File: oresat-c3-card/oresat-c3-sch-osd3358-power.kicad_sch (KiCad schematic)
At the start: 39 parts, among them Q6 MMBT2907, U1 OSD3358-1G-ISM, U10 SN74AUC1G07DCKR, U14 TLVH431

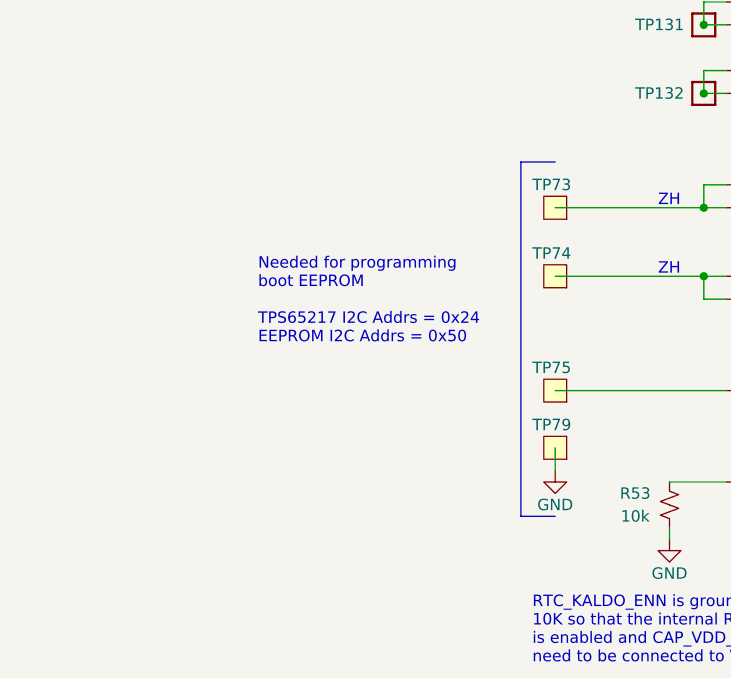
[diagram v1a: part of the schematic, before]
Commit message: schematic changes following design review
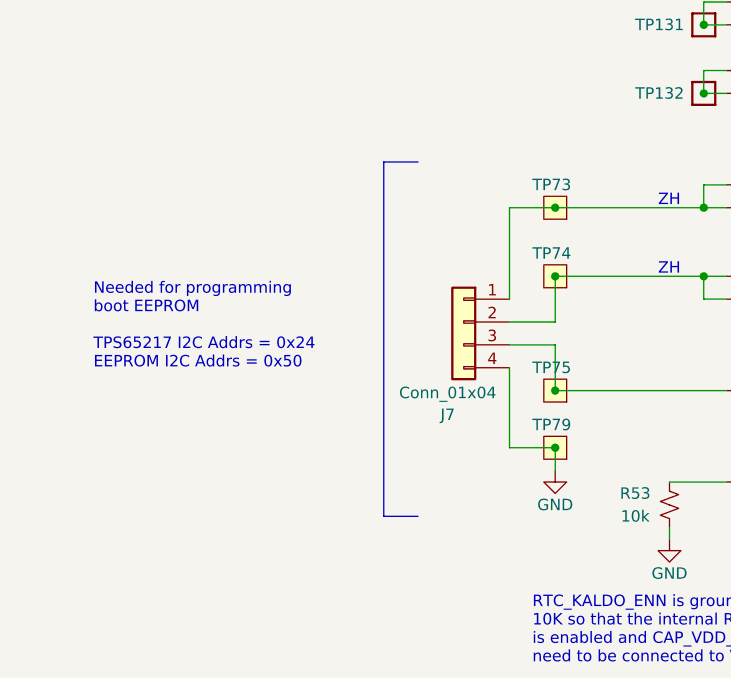
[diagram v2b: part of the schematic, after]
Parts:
- added J7: Conn_01x04, symbol Connector_Generic:Conn_01x04
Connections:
- net GND: now also J7.4 (Pin_4)
- net at TP75.1, U1.M2 (EEPROM_WP): now also J7.3 (Pin_3)
- net at TP74.1, U1.C11 (I2C0_SDA), U1.D11 (PMIC_SDA): now also J7.2 (Pin_2)
- net at TP73.1, U1.C10 (I2C0_SCL), U1.D10 (PMIC_SCL): now also J7.1 (Pin_1)
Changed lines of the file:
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@@
 	(text "Needed for programming\nboot EEPROM\n\nTPS65217 I2C Addrs = 0x24\nEEPROM I2C Addrs = 0x50"
 		(exclude_from_sim no)
-		(at 137.16 200.66 0)
+		(at 118.872 203.454 0)
 		(effects
 			(font
@@
 	)
 	(junction
+		(at 170.18 205.74)
+		(diameter 0)
+		(color 0 0 0 0)
+	)
+	(junction
 		(at 186.69 55.88)
 		(diameter 0)
@@
 	)
 	(junction
+		(at 170.18 185.42)
+		(diameter 0)
+		(color 0 0 0 0)
+	)
+	(junction
 		(at 265.43 157.48)
 		(diameter 0)
@@
 	)
 	(junction
+		(at 170.18 212.09)
+		(diameter 0)
+		(color 0 0 0 0)
+	)
+	(junction
 		(at 292.1 215.9)
 		(diameter 0)
@@
 	)
 	(junction
+		(at 170.18 193.04)
+		(diameter 0)
+		(color 0 0 0 0)
+	)
+	(junction
 		(at 265.43 149.86)
 		(diameter 0)
@@
 	(wire
 		(pts
+			(xy 170.18 200.66) (xy 170.18 205.74)
+		)
+		(stroke
+			(width 0)
+			(type default)
+		)
+	)
+	(wire
+		(pts
 			(xy 299.72 207.01) (xy 299.72 208.28)
 		)
@@
 	(polyline
 		(pts
-			(xy 166.37 219.71) (xy 170.18 219.71)
+			(xy 151.13 219.71) (xy 154.94 219.71)
 		)
 		(stroke
@@
 	(polyline
 		(pts
-			(xy 170.18 180.34) (xy 166.37 180.34)
+			(xy 154.94 180.34) (xy 151.13 180.34)
 		)
 		(stroke
@@
 	(wire
 		(pts
+			(xy 165.1 195.58) (xy 165.1 185.42)
+		)
+		(stroke
+			(width 0)
+			(type default)
+		)
+	)
+	(wire
+		(pts
 			(xy 186.69 162.56) (xy 186.69 165.1)
 		)
@@
 	(wire
 		(pts
+			(xy 165.1 200.66) (xy 170.18 200.66)
+		)
+		(stroke
+			(width 0)
+			(type default)
+		)
+	)
+	(wire
+		(pts
 			(xy 186.69 88.9) (xy 189.23 88.9)
 		)
@@
 	(wire
 		(pts
+			(xy 165.1 212.09) (xy 170.18 212.09)
+		)
+		(stroke
+			(width 0)
+			(type default)
+		)
+	)
+	(wire
+		(pts
 			(xy 265.43 180.34) (xy 265.43 177.8)
 		)
@@
 	(wire
 		(pts
+			(xy 170.18 198.12) (xy 170.18 193.04)
+		)
+		(stroke
+			(width 0)
+			(type default)
+		)
+	)
+	(wire
+		(pts
 			(xy 260.35 127) (xy 265.43 127)
 		)
@@
 	(polyline
 		(pts
-			(xy 166.37 180.34) (xy 166.37 219.71)
+			(xy 151.13 180.34) (xy 151.13 219.71)
 		)
 		(stroke
@@
 	(wire
 		(pts
+			(xy 165.1 185.42) (xy 170.18 185.42)
+		)
+		(stroke
+			(width 0)
+			(type default)
+		)
+	)
+	(wire
+		(pts
 			(xy 308.61 149.86) (xy 298.45 149.86)
 		)
@@
 	(wire
 		(pts
+			(xy 165.1 203.2) (xy 165.1 212.09)
+		)
+		(stroke
+			(width 0)
+			(type default)
+		)
+	)
+	(wire
+		(pts
+			(xy 165.1 198.12) (xy 170.18 198.12)
+		)
+		(stroke
+			(width 0)
+			(type default)
+		)
+	)
+	(wire
+		(pts
 			(xy 312.42 104.14) (xy 312.42 185.42)
 		)
@@
 					(unit 1)
 				)
+			)
+		)
+	)
+	(symbol
+		(lib_id "Connector_Generic:Conn_01x04")
+		(at 160.02 198.12 0)
+		(mirror y)
+		(unit 1)
+		(exclude_from_sim no)
+		(in_bom yes)
+		(on_board yes)
+		(dnp no)
+		(property "Reference" "J7"
+			(at 158.242 208.4183 0)
+			(effects
+				(font
+					(size 1.27 1.27)
+				)
+			)
+		)
+		(property "Value" "Conn_01x04"
+			(at 158.242 205.994 0)
+			(effects
+				(font
+					(size 1.27 1.27)
+				)
+			)
+		)
+		(property "Footprint" ""
+			(at 160.02 198.12 0)
+			(effects
+				(font
+					(size 1.27 1.27)
+				)
+				(hide yes)
+			)
+		)
+		(property "Datasheet" "~"
+			(at 160.02 198.12 0)
+			(effects
+				(font
+					(size 1.27 1.27)
+				)
+				(hide yes)
+			)
+		)
+		(property "Description" "Generic connector, single row, 01x04, script generated (kicad-library-utils/schlib/autogen/connector/)"
+			(at 160.02 198.12 0)
+			(effects
+				(font
+					(size 1.27 1.27)
+				)
+				(hide yes)
+			)
+		)
+		(pin "4"
+		)
+		(pin "3"
+		)
+		(pin "1"
+		)
+		(pin "2"
+		)
+		(instances
+			(project ""
+				(path "/65d12cdd-c326-4033-9053-c59fa4e0b25e/0c1da208-2d1c-4d05-9cc7-59584e50a6ac"
+					(reference "J7")
+					(unit 1)
+				)

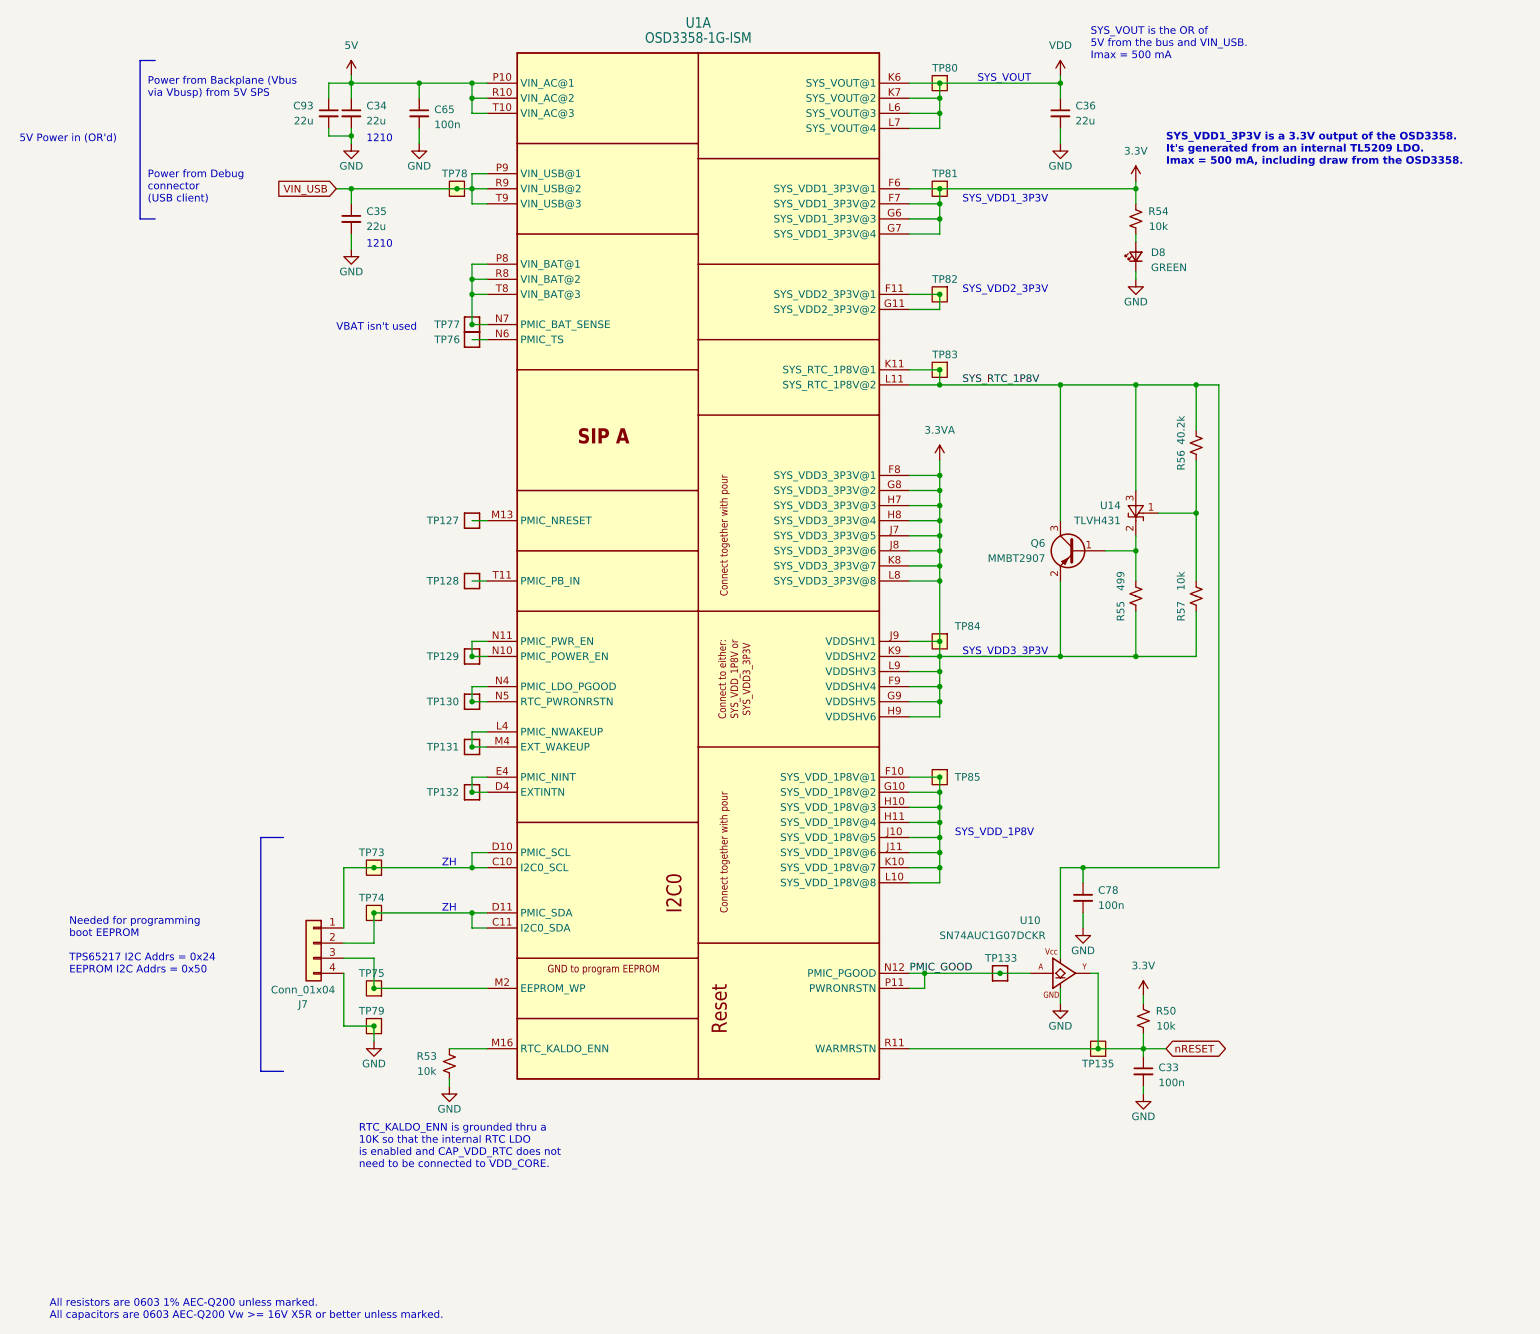
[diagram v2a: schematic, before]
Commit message: Additional C3 design review changes and routing progress
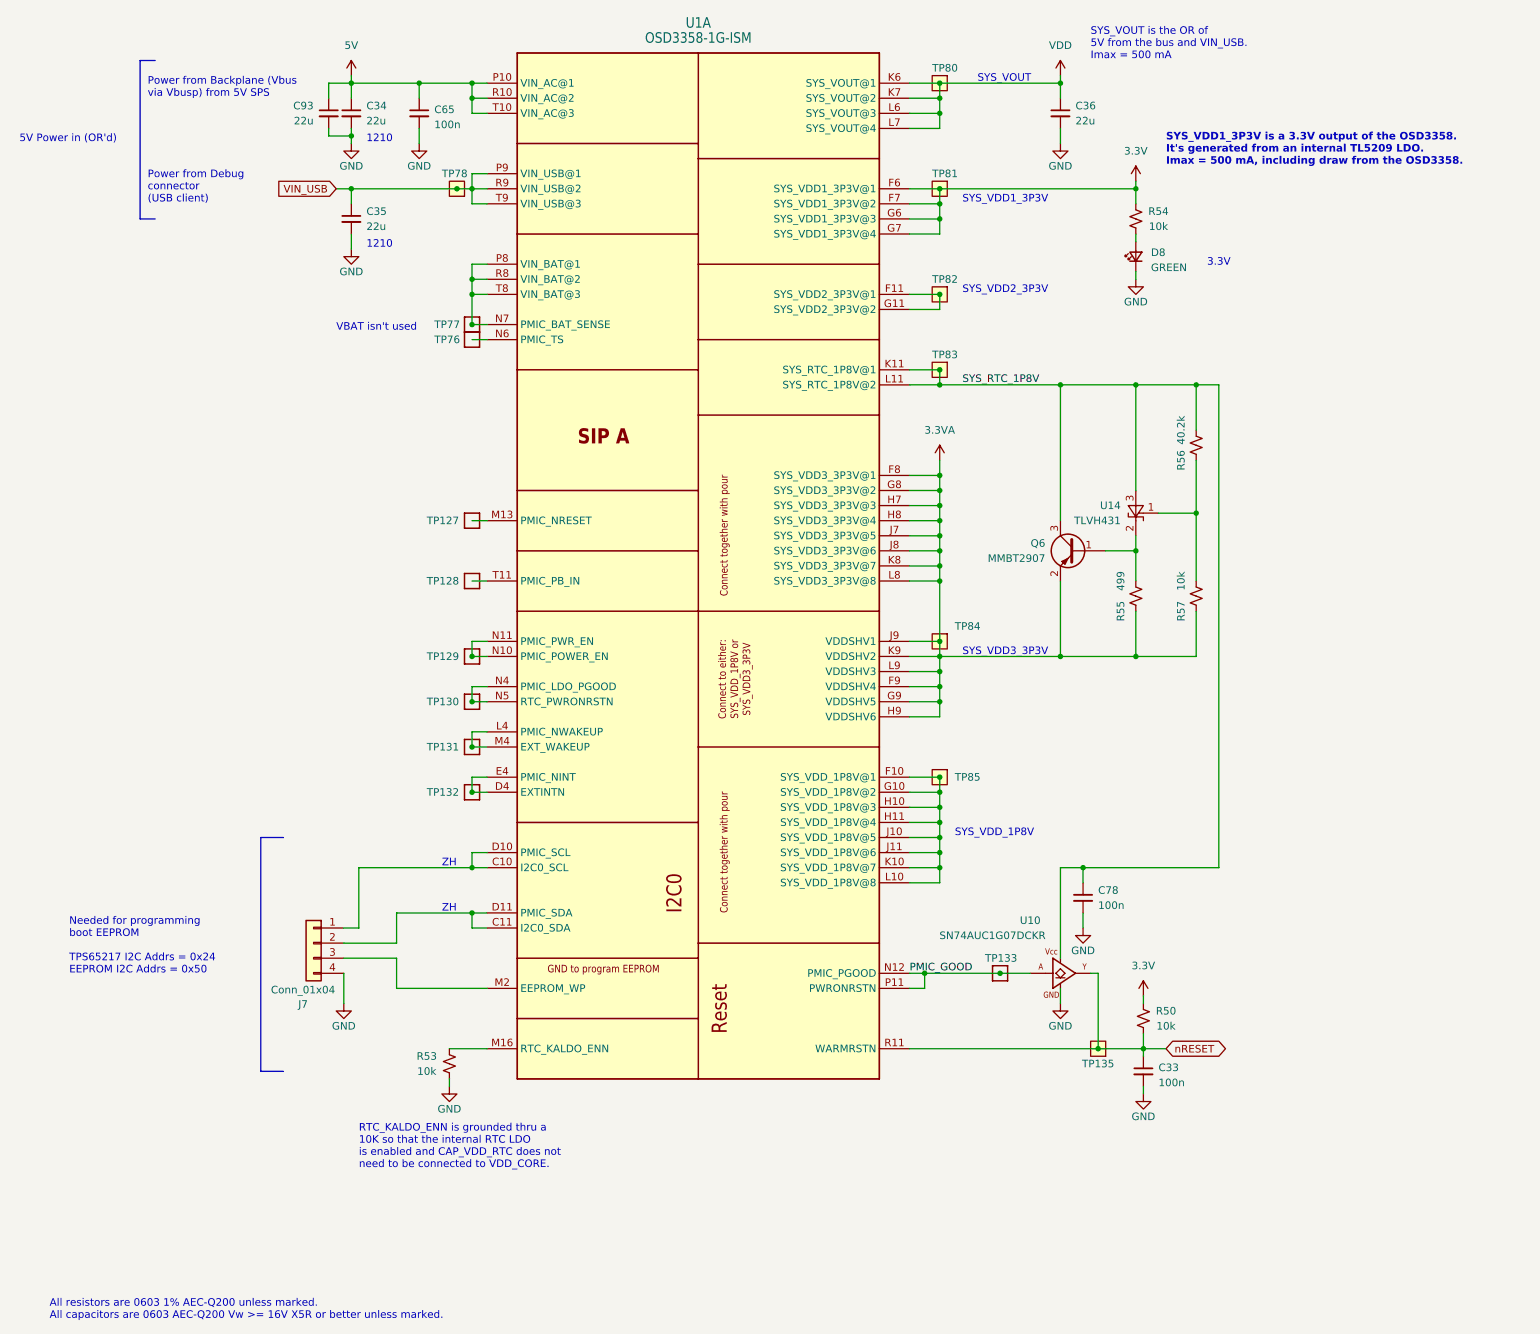
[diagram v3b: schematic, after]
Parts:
- removed TP73, TP74, TP75, TP79: Test-Point, oresat-misc:TestPoint-0.75mm-th, symbol oresat-misc:Test-Point-0.75mm-th
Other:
- note added: "3.3V"

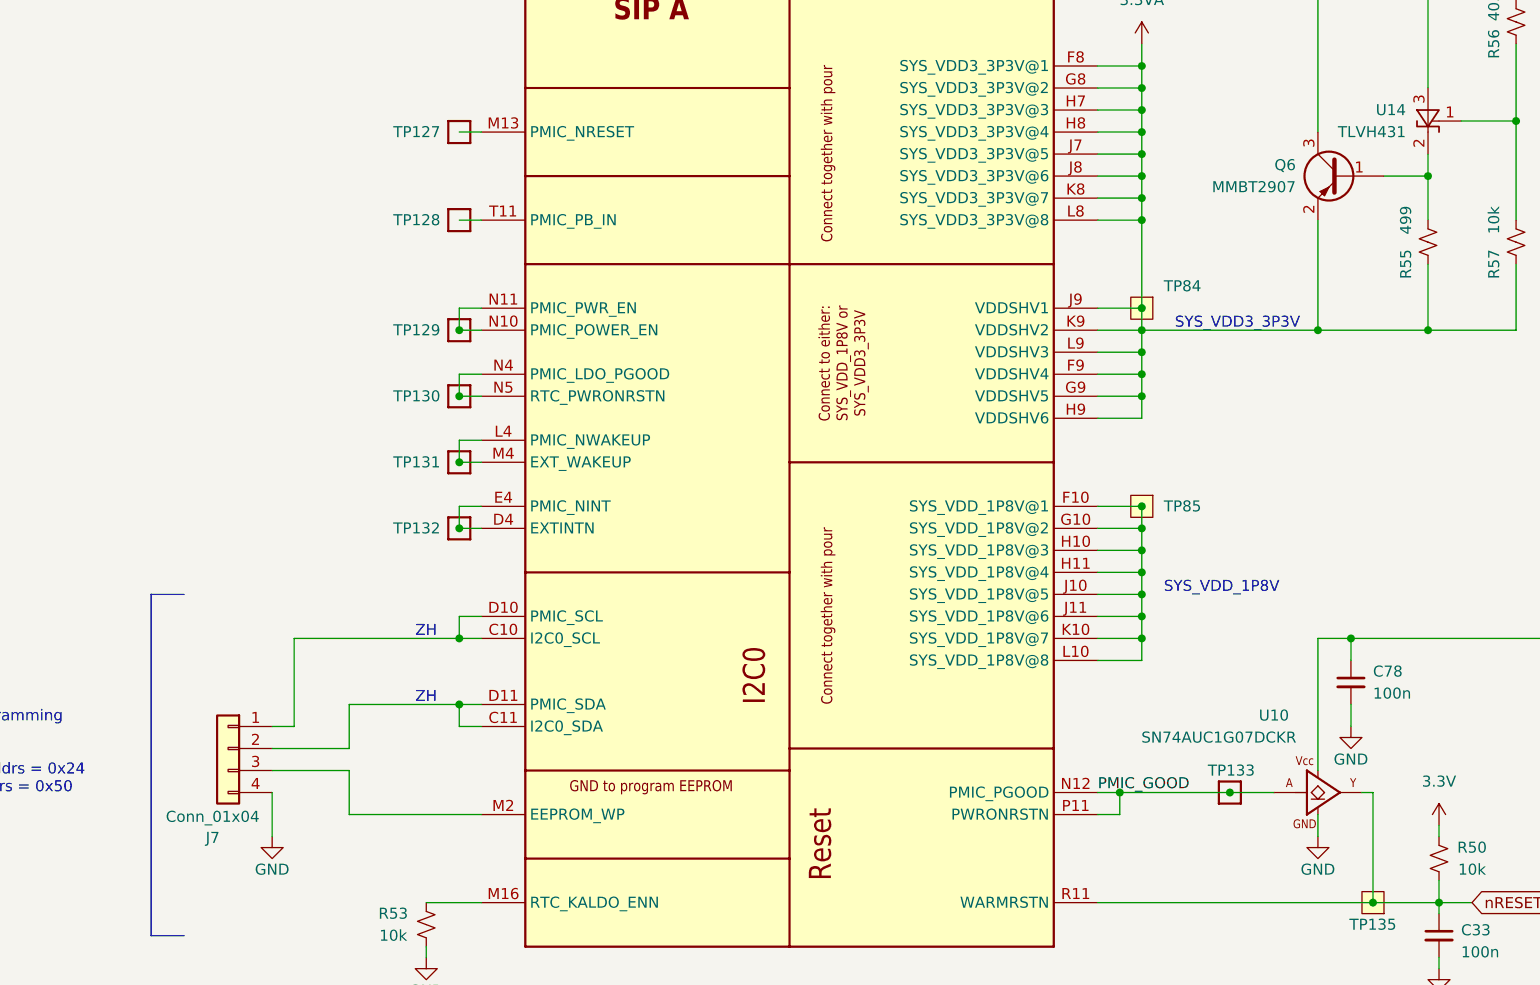
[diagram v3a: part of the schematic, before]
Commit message: completed rough rounting on left side and l band rf side
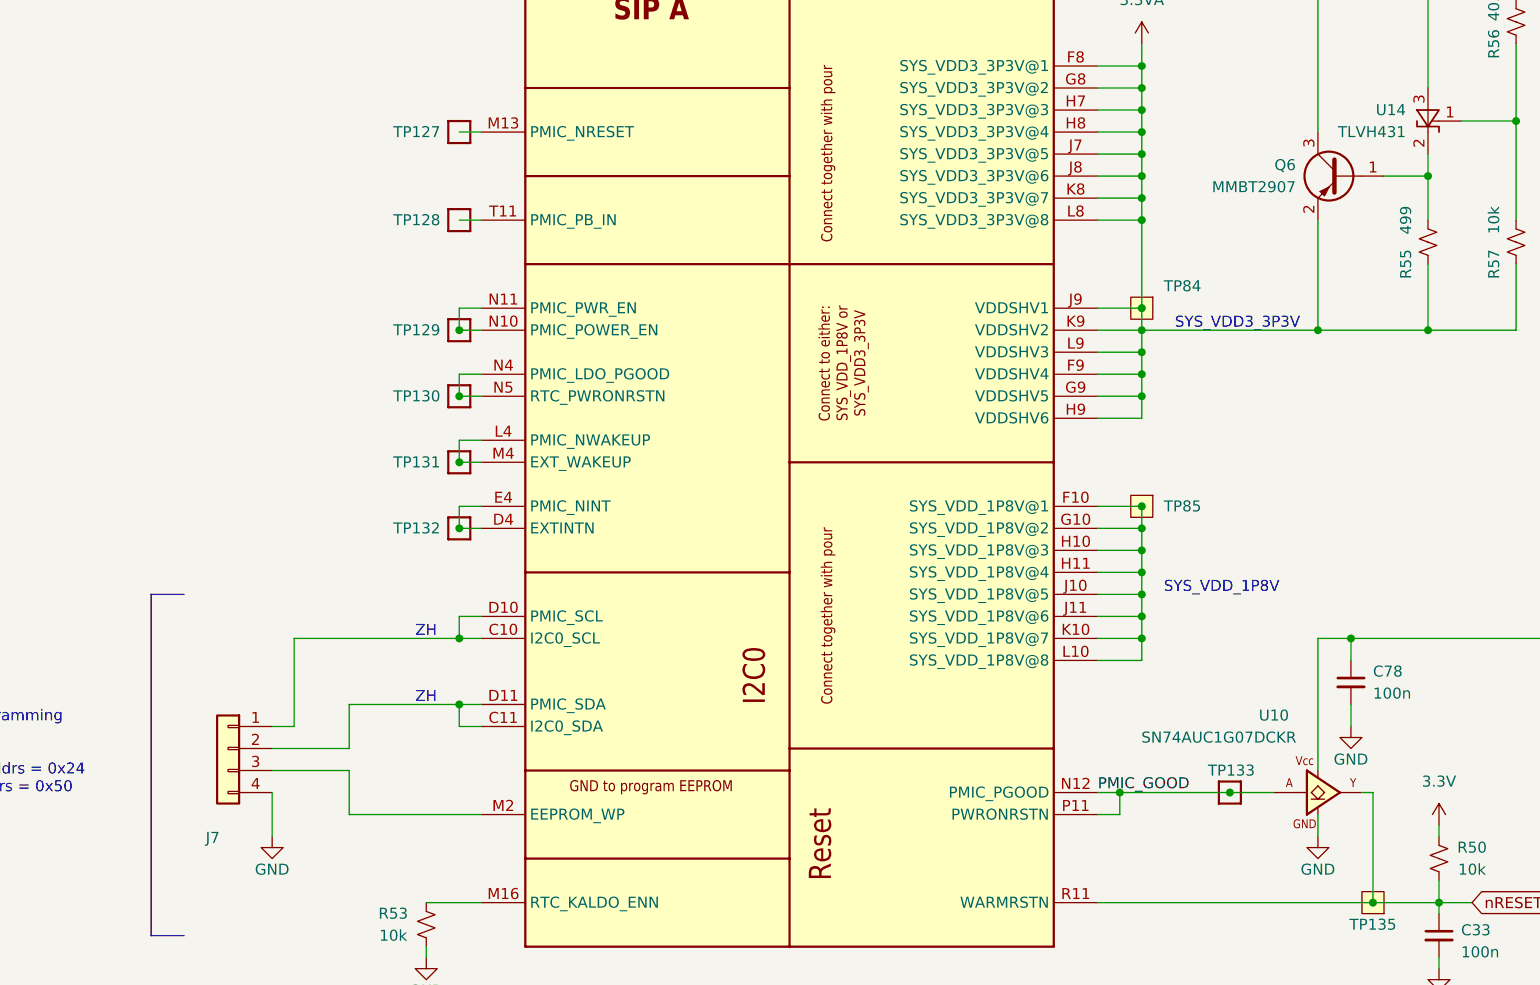
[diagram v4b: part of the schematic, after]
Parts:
- J7: value Conn_01x04 -> ~; footprint (none) -> Connector_PinHeader_1.27mm:PinHeader_1x04_P1.27mm_Vertical
- Q6: symbol Device:Q_PNP_BEC -> Transistor_BJT:Q_PNP_BEC
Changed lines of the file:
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@@
 			)
 		)
-		(property "Description" "Green 520nm LED Indication - Discrete 3.2V 0603 (1608 Metric) - 430 mcd @ 20 mA"
+		(property "Description" "Light emitting diode, small symbol"
 			(at 298.45 82.55 0)
 			(effects
@@
 			)
 		)
+		(property "Sim.Pin" "1=K 2=A"
+			(at 298.45 82.55 0)
+			(effects
+				(font
+					(size 1.27 1.27)
+				)
+				(hide yes)
+			)
+		)
 		(pin "1"
 		)
@@
 			)
 		)
-		(property "Value" "Conn_01x04"
+		(property "Value" "~"
 			(at 158.242 205.994 0)
 			(effects
@@
 			)
 		)
-		(property "Footprint" ""
+		(property "Footprint" "Connector_PinHeader_1.27mm:PinHeader_1x04_P1.27mm_Vertical"
 			(at 160.02 198.12 0)
 			(effects
@@
 	)
 	(symbol
-		(lib_id "Device:Q_PNP_BEC")
+		(lib_id "Transistor_BJT:Q_PNP_BEC")
 		(at 288.29 132.08 0)
 		(mirror y)
@@
 		)
 		(property "Footprint" "Package_TO_SOT_SMD:SOT-353_SC-70-5"
-			(at 285.75 203.2 0)
+			(at 285.75 193.04 0)
 			(effects
 				(font
@@
 		)
 		(property "Datasheet" "https://www.ti.com/lit/ds/symlink/sn74lvc1g07.pdf"
-			(at 285.75 203.2 0)
+			(at 285.75 195.58 0)
 			(effects
 				(font
@@
 			)
 		)
-		(property "Description" "Buffer, Non-Inverting 1 Element 1 Bit per Element Open Drain Output SC-70-5"
+		(property "Description" "Single Buffer, SC-70-5"
 			(at 285.75 203.2 0)
 			(effects
